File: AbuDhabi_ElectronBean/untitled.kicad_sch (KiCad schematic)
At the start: 2 parts

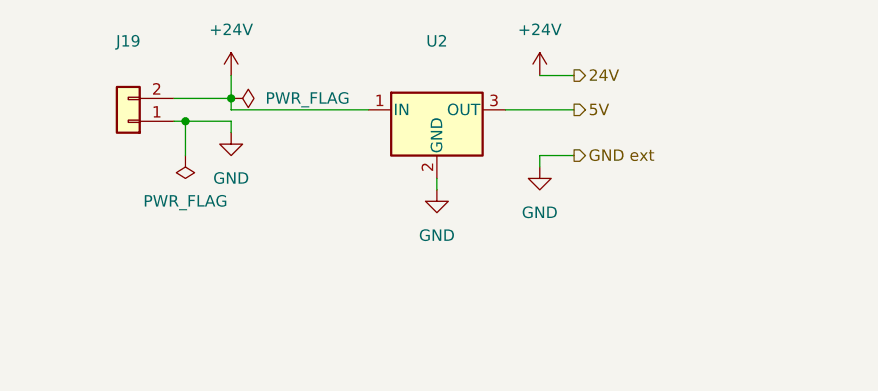
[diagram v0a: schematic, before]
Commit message: Arduino Mega footpring change and LEDs addition
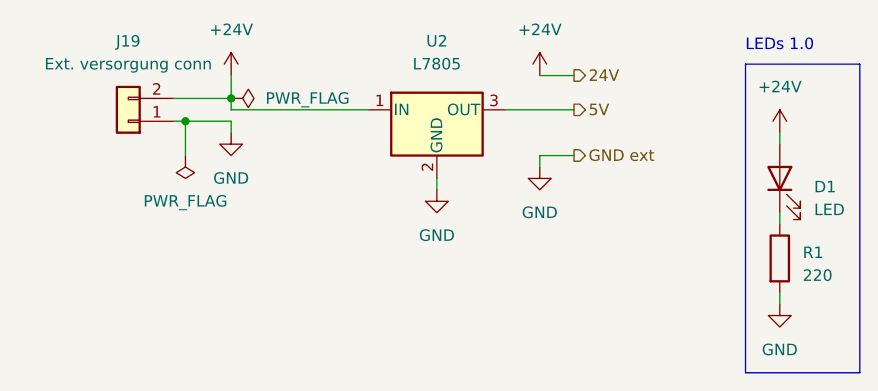
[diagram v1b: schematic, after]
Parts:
- added D1: LED, LED_SMD:LED_0603_1608Metric_Pad1.05x0.95mm_HandSolder, symbol Device:LED
- added R1: 220, Resistor_SMD:R_0805_2012Metric_Pad1.20x1.40mm_HandSolder, symbol Device:R
- J19: value (none) -> Ext. versorgung conn; footprint (none) -> Connector_JST:JST_EH_B2B-EH-A_1x02_P2.50mm_Vertical
- U2: value (none) -> L7805; footprint (none) -> Package_TO_SOT_THT:TO-220-3_Vertical
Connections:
- net +24V: now also D1.2 (A)
- net GND: now also R1.2
- new net: D1.1 (K), R1.1
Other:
- note added: "LEDs 1.0"

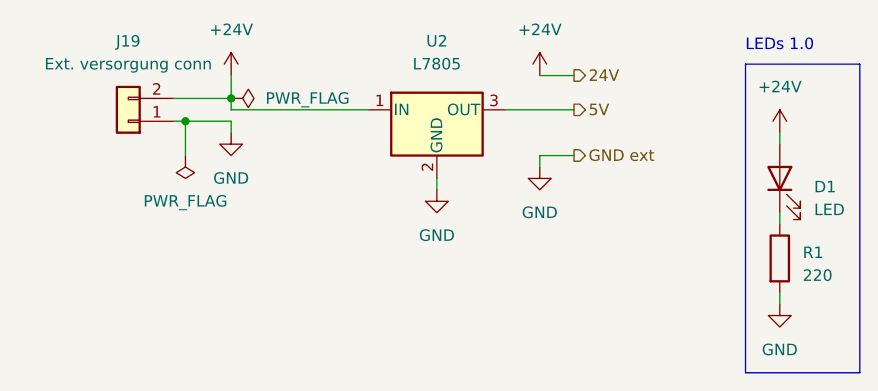
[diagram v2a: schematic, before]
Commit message: Main board file updated. Added Arduino code for the LCD
The LCD is not working yet though.
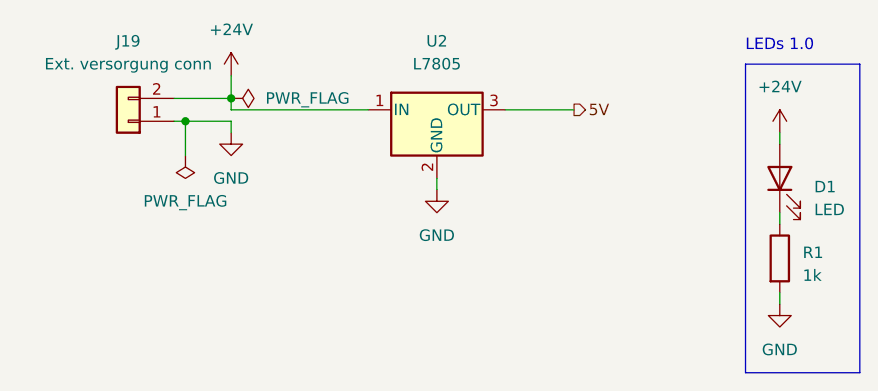
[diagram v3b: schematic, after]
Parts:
- R1: value 220 -> 1k; footprint Resistor_SMD:R_0805_2012Metric_Pad1.20x1.40mm_HandSolder -> Resistor_SMD:R_0603_1608Metric
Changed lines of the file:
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@@
   (junction (at 30.48 24.13) (diameter 0) (color 0 0 0 0)
   )
-  (wire (pts (xy 69.85 27.94) (xy 73.66 27.94))
-    (stroke (width 0) (type default))
-  )
   (wire (pts (xy 30.48 24.13) (xy 35.56 24.13))
     (stroke (width 0) (type default))
@@
   )
   (wire (pts (xy 35.56 24.13) (xy 35.56 25.4))
-    (stroke (width 0) (type default))
-  )
-  (wire (pts (xy 69.85 19.05) (xy 73.66 19.05))
     (stroke (width 0) (type default))
   )
@@
     (stroke (width 0) (type default))
   )
-  (wire (pts (xy 69.85 29.21) (xy 69.85 27.94))
-    (stroke (width 0) (type default))
-  )
   (text "LEDs 1.0" (at 100.33 16.51 0)
     (effects (font (size 1.27 1.27)) (justify right bottom))
@@
   (hierarchical_label "5V" (shape output) (at 73.66 22.86 0) (fields_autoplaced)
     (effects (font (size 1.27 1.27)) (justify left))
-  )
-  (hierarchical_label "24V" (shape output) (at 73.66 19.05 0) (fields_autoplaced)
-    (effects (font (size 1.27 1.27)) (justify left))
-  )
-  (hierarchical_label "GND ext" (shape output) (at 73.66 27.94 0) (fields_autoplaced)
-    (effects (font (size 1.27 1.27)) (justify left))
-  )
-  (symbol (lib_id "power:+24V") (at 69.85 19.05 0) (unit 1)
-    (in_bom yes) (on_board yes) (dnp no) (fields_autoplaced)
-    (property "Reference" "#PWR0109" (at 69.85 22.86 0)
-      (effects (font (size 1.27 1.27)) hide)
-    )
-    (property "Value" "+24V" (at 69.85 13.97 0)
-      (effects (font (size 1.27 1.27)))
-    )
-    (property "Footprint" "" (at 69.85 19.05 0)
-      (effects (font (size 1.27 1.27)) hide)
-    )
-    (property "Datasheet" "" (at 69.85 19.05 0)
-      (effects (font (size 1.27 1.27)) hide)
-    )
-    (pin "1")
-    (instances
-      (project "AbuDhabi_ElectronBean"
-        (path "/e63e39d7-6ac0-4ffd-8aa3-1841a4541b55/c90f5046-40eb-4e2a-9cc6-7f8f7a86d6fc"
-          (reference "#PWR0109") (unit 1)
-        )
-      )
-    )
   )
   (symbol (lib_id "power:PWR_FLAG") (at 35.56 21.59 270) (unit 1)
@@
     (pin "1")
     (instances
-      (project "AbuDhabi_ElectronBean"
+      (project "AbuDhabi_ElectronBeam"
         (path "/e63e39d7-6ac0-4ffd-8aa3-1841a4541b55/c90f5046-40eb-4e2a-9cc6-7f8f7a86d6fc"
           (reference "#FLG0101") (unit 1)
@@
     (pin "1")
     (instances
-      (project "AbuDhabi_ElectronBean"
+      (project "AbuDhabi_ElectronBeam"
         (path "/e63e39d7-6ac0-4ffd-8aa3-1841a4541b55/c90f5046-40eb-4e2a-9cc6-7f8f7a86d6fc"
           (reference "#PWR0108") (unit 1)
@@
       (effects (font (size 1.27 1.27)) (justify left))
     )
-    (property "Value" "220" (at 99.06 41.275 0)
+    (property "Value" "1k" (at 99.06 41.275 0)
       (effects (font (size 1.27 1.27)) (justify left))
     )
-    (property "Footprint" "Resistor_SMD:R_0805_2012Metric_Pad1.20x1.40mm_HandSolder" (at 94.742 39.37 90)
+    (property "Footprint" "Resistor_SMD:R_0603_1608Metric" (at 94.742 39.37 90)
       (effects (font (size 1.27 1.27)) hide)
     )
@@
     (pin "2")
     (instances
-      (project "AbuDhabi_ElectronBean"
+      (project "AbuDhabi_ElectronBeam"
         (path "/e63e39d7-6ac0-4ffd-8aa3-1841a4541b55"
           (reference "R1") (unit 1)
@@
     (pin "3")
     (instances
-      (project "AbuDhabi_ElectronBean"
+      (project "AbuDhabi_ElectronBeam"
         (path "/e63e39d7-6ac0-4ffd-8aa3-1841a4541b55/c90f5046-40eb-4e2a-9cc6-7f8f7a86d6fc"
           (reference "U2") (unit 1)
@@
     (pin "1")
     (instances
-      (project "AbuDhabi_ElectronBean"
+      (project "AbuDhabi_ElectronBeam"
         (path "/e63e39d7-6ac0-4ffd-8aa3-1841a4541b55/c90f5046-40eb-4e2a-9cc6-7f8f7a86d6fc"
           (reference "#PWR0103") (unit 1)
@@
     (pin "1")
     (instances
-      (project "AbuDhabi_ElectronBean"
+      (project "AbuDhabi_ElectronBeam"
         (path "/e63e39d7-6ac0-4ffd-8aa3-1841a4541b55/c90f5046-40eb-4e2a-9cc6-7f8f7a86d6fc"
           (reference "#PWR010") (unit 1)
@@
     (pin "1")
     (instances
-      (project "AbuDhabi_ElectronBean"
+      (project "AbuDhabi_ElectronBeam"
         (path "/e63e39d7-6ac0-4ffd-8aa3-1841a4541b55/c90f5046-40eb-4e2a-9cc6-7f8f7a86d6fc"
           (reference "#FLG0102") (unit 1)
@@
     (pin "2")
     (instances
-      (project "AbuDhabi_ElectronBean"
+      (project "AbuDhabi_ElectronBeam"
         (path "/e63e39d7-6ac0-4ffd-8aa3-1841a4541b55"
           (reference "D1") (unit 1)
@@
     (pin "1")
     (instances
-      (project "AbuDhabi_ElectronBean"
+      (project "AbuDhabi_ElectronBeam"
         (path "/e63e39d7-6ac0-4ffd-8aa3-1841a4541b55"
           (reference "#PWR08") (unit 1)
@@
     (pin "1")
     (instances
-      (project "AbuDhabi_ElectronBean"
+      (project "AbuDhabi_ElectronBeam"
         (path "/e63e39d7-6ac0-4ffd-8aa3-1841a4541b55/c90f5046-40eb-4e2a-9cc6-7f8f7a86d6fc"
           (reference "#PWR0102") (unit 1)
@@
     )
   )
-  (symbol (lib_id "power:GND") (at 69.85 29.21 0) (unit 1)
-    (in_bom yes) (on_board yes) (dnp no) (fields_autoplaced)
-    (property "Reference" "#PWR0104" (at 69.85 35.56 0)
-      (effects (font (size 1.27 1.27)) hide)
-    )
-    (property "Value" "GND" (at 69.85 34.29 0)
-      (effects (font (size 1.27 1.27)))
-    )
-    (property "Footprint" "" (at 69.85 29.21 0)
-      (effects (font (size 1.27 1.27)) hide)
-    )
-    (property "Datasheet" "" (at 69.85 29.21 0)
-      (effects (font (size 1.27 1.27)) hide)
-    )
-    (pin "1")
-    (instances
-      (project "AbuDhabi_ElectronBean"
-        (path "/e63e39d7-6ac0-4ffd-8aa3-1841a4541b55/c90f5046-40eb-4e2a-9cc6-7f8f7a86d6fc"
-          (reference "#PWR0104") (unit 1)
-        )
-      )
-    )
-  )
   (symbol (lib_id "Connector_Generic:Conn_01x02") (at 24.13 24.13 180) (unit 1)
     (in_bom yes) (on_board yes) (dnp no) (fields_autoplaced)
@@
     (pin "2")
     (instances
-      (project "AbuDhabi_ElectronBean"
+      (project "AbuDhabi_ElectronBeam"
         (path "/e63e39d7-6ac0-4ffd-8aa3-1841a4541b55/c90f5046-40eb-4e2a-9cc6-7f8f7a86d6fc"
           (reference "J19") (unit 1)
